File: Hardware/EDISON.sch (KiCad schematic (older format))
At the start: 5 parts, among them P5 CONN_01X06, SW2 PWR_BTN, U18 EdisonConnector

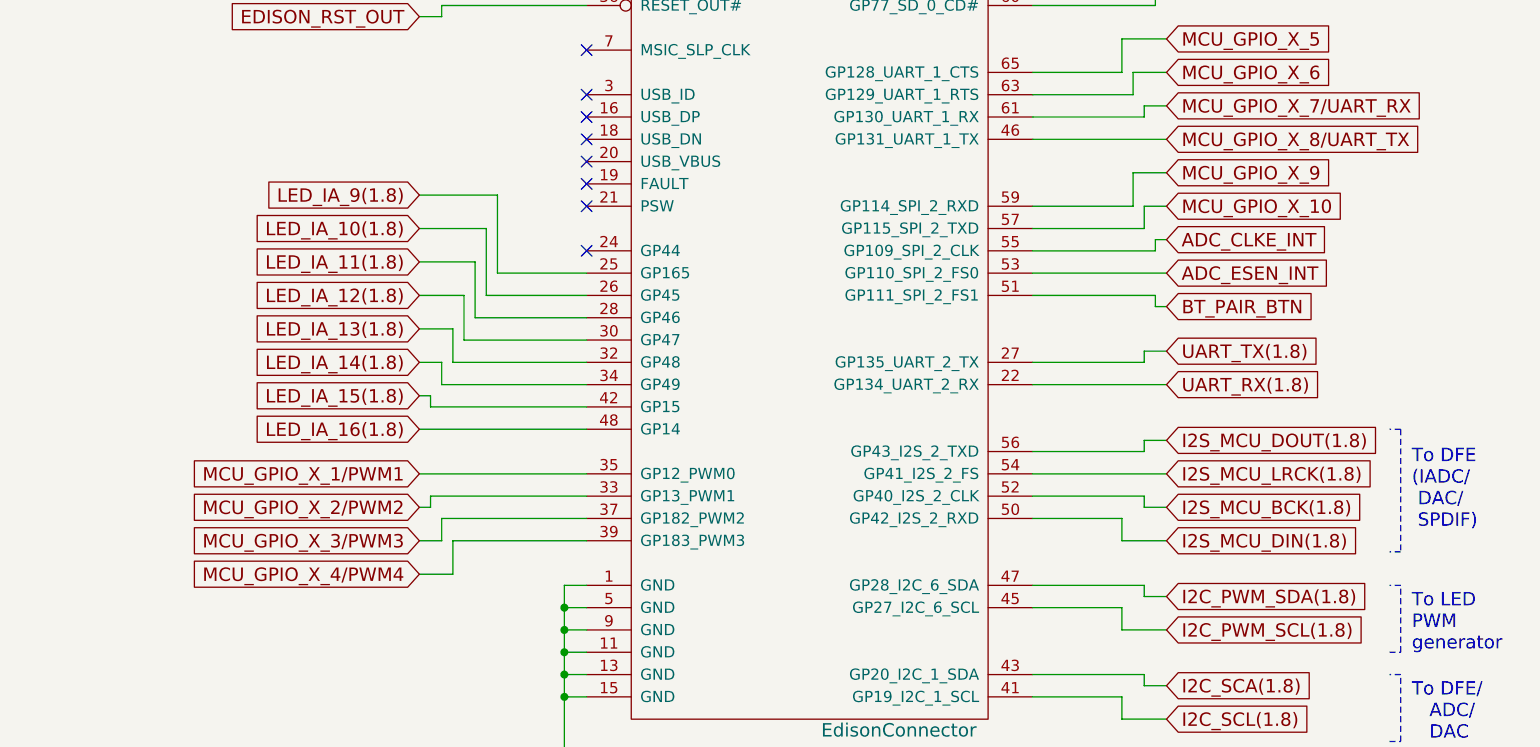
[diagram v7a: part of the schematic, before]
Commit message: Fixed schematic errors, added muse-v2-lib
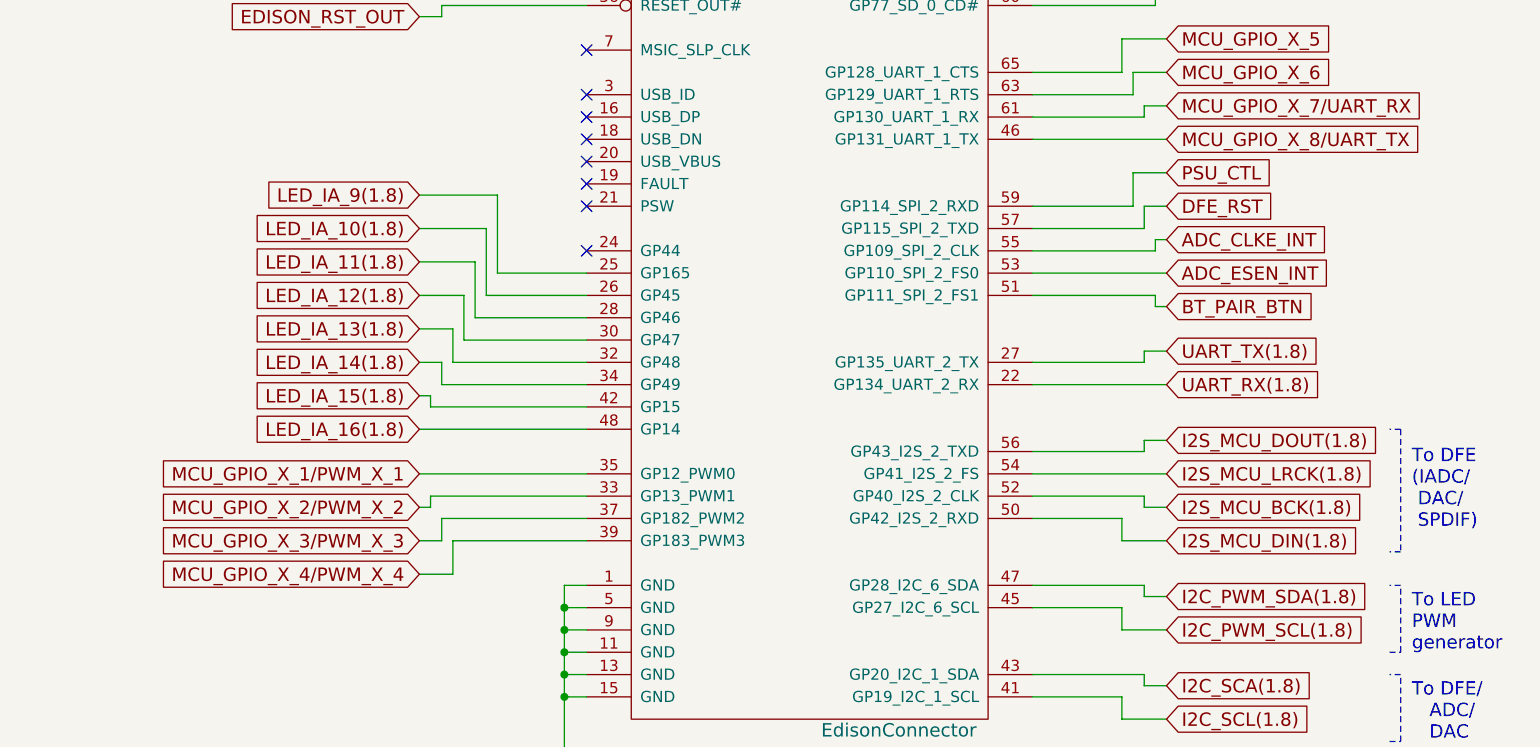
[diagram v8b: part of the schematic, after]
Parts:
- P5: footprint (none) -> Pin_Headers:Pin_Header_Straight_1x06
- R127, R128: footprint (none) -> Resistors_SMD:R_0402
- SW2: footprint (none) -> MF_Switches:MF_Switches-TACT4.2MM
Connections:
- net MCU_GPIO_X_1/PWM1 renamed MCU_GPIO_X_1/PWM_X_1
- net MCU_GPIO_X_10 renamed DFE_RST
- net MCU_GPIO_X_2/PWM2 renamed MCU_GPIO_X_2/PWM_X_2
- net MCU_GPIO_X_3/PWM3 renamed MCU_GPIO_X_3/PWM_X_3
- net MCU_GPIO_X_4/PWM4 renamed MCU_GPIO_X_4/PWM_X_4
- net MCU_GPIO_X_9 renamed PSU_CTL
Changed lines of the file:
@@
 F 0 "U18" H 3700 1600 60  0000 C CNN
 F 1 "EdisonConnector" H 4850 -3000 60  0000 C CNN
-F 2 "" H 3650 1950 60  0000 C CNN
+F 2 "" H 3650 1950 60  0001 C CNN
 F 3 "" H 3650 1950 60  0000 C CNN
 	1    3650 1550
@@
 To DFE\n(IADC/\n DAC/\n SPDIF)
 $Comp
-L +1.8VSB #PWR097
+L +1.8VSB #PWR106
 U 1 1 57F8CABA
 P 3150 1400
-F 0 "#PWR097" H 3150 1540 20  0001 C CNN
+F 0 "#PWR106" H 3150 1540 20  0001 C CNN
 F 1 "+1.8VSB" H 3150 1510 30  0000 C CNN
 F 2 "" H 3150 1400 60  0000 C CNN
@@
 $EndComp
 $Comp
-L +3.3VSB #PWR098
+L +3.3VSB #PWR107
 U 1 1 57F8CAC0
 P 3350 1400
-F 0 "#PWR098" H 3350 1360 30  0001 C CNN
+F 0 "#PWR107" H 3350 1360 30  0001 C CNN
 F 1 "+3.3VSB" H 3350 1510 30  0000 C CNN
 F 2 "" H 3350 1400 60  0000 C CNN
@@
 NoConn ~ 1250 1750
 $Comp
-L GND-RESCUE-museV2-RESCUE-museV2 #PWR099
+L GND-RESCUE-museV2-RESCUE-museV2 #PWR108
 U 1 1 57F8CACB
 P 1350 2050
-F 0 "#PWR099" H 1350 2050 30  0001 C CNN
+F 0 "#PWR108" H 1350 2050 30  0001 C CNN
 F 1 "GND" H 1350 1980 30  0001 C CNN
 F 2 "" H 1350 2050 60  0000 C CNN
@@
 F 0 "P5" H 1050 2050 50  0000 C CNN
 F 1 "CONN_01X06" V 1150 1700 50  0000 C CNN
-F 2 "" H 1050 1700 60  0000 C CNN
+F 2 "Pin_Headers:Pin_Header_Straight_1x06" H 1050 1700 60  0001 C CNN
 F 3 "" H 1050 1700 60  0000 C CNN
 	1    1050 1700
@@
 Intel Edison Connection
 $Comp
-L GND-RESCUE-museV2-RESCUE-museV2 #PWR0100
+L GND-RESCUE-museV2-RESCUE-museV2 #PWR109
 U 1 1 57F8CAEE
 P 3350 6200
-F 0 "#PWR0100" H 3350 6200 30  0001 C CNN
+F 0 "#PWR109" H 3350 6200 30  0001 C CNN
 F 1 "GND" H 3350 6130 30  0001 C CNN
 F 2 "" H 3350 6200 60  0000 C CNN
@@
 MCU_GPIO_X_8/UART_TX
 Text GLabel 6050 3600 2    60   Input ~ 0
-MCU_GPIO_X_9
+PSU_CTL
 Text GLabel 6050 3750 2    60   Input ~ 0
-MCU_GPIO_X_10
+DFE_RST
 Text GLabel 6050 3900 2    60   Input ~ 0
 ADC_CLKE_INT
@@
 	3050 3700 2700 3700
 Text GLabel 2700 4950 0    60   Input ~ 0
-MCU_GPIO_X_1/PWM1
+MCU_GPIO_X_1/PWM_X_1
 Wire Wire Line
 	2700 4950 3450 4950
 Text GLabel 2700 5100 0    60   Input ~ 0
-MCU_GPIO_X_2/PWM2
+MCU_GPIO_X_2/PWM_X_2
 Text GLabel 2700 5250 0    60   Input ~ 0
-MCU_GPIO_X_3/PWM3
+MCU_GPIO_X_3/PWM_X_3
 Text GLabel 2700 5400 0    60   Input ~ 0
-MCU_GPIO_X_4/PWM4
+MCU_GPIO_X_4/PWM_X_4
 Wire Wire Line
 	2700 5100 2750 5100
@@
 	2850 5250 3450 5250
 $Comp
-L GND-RESCUE-museV2-RESCUE-museV2 #PWR0101
+L GND-RESCUE-museV2-RESCUE-museV2 #PWR111
 U 1 1 58589956
 P 1150 8600
-F 0 "#PWR0101" H 1150 8600 30  0001 C CNN
+F 0 "#PWR111" H 1150 8600 30  0001 C CNN
 F 1 "GND" H 1150 8530 30  0001 C CNN
 F 2 "" H 1150 8600 60  0000 C CNN
@@
 F 0 "R127" V 1230 7200 40  0000 C CNN
 F 1 "10K" V 1157 7201 40  0000 C CNN
-F 2 "" V 1080 7200 30  0000 C CNN
+F 2 "Resistors_SMD:R_0402" V 1080 7200 30  0001 C CNN
 F 3 "" H 1150 7200 30  0000 C CNN
 	1    1150 7200
@@
 F 0 "SW2" H 1300 7960 50  0000 C CNN
 F 1 "PWR_BTN" H 1150 7770 50  0000 C CNN
-F 2 "" H 1150 7850 60  0000 C CNN
+F 2 "MF_Switches:MF_Switches-TACT4.2MM" H 1150 7850 60  0001 C CNN
 F 3 "" H 1150 7850 60  0000 C CNN
 	1    1150 7850
@@
 F 0 "R128" V 1430 7200 40  0000 C CNN
 F 1 "220" V 1357 7201 40  0000 C CNN
-F 2 "" V 1280 7200 30  0000 C CNN
+F 2 "Resistors_SMD:R_0402" V 1280 7200 30  0001 C CNN
 F 3 "" H 1350 7200 30  0000 C CNN
 	1    1350 7200
@@
 	1350 7450 1150 7450
 $Comp
-L +3.3VSB #PWR0102
+L +3.3VSB #PWR110
 U 1 1 58589976
 P 1150 6750
-F 0 "#PWR0102" H 1150 6710 30  0001 C CNN
+F 0 "#PWR110" H 1150 6710 30  0001 C CNN
 F 1 "+3.3VSB" H 1150 6860 30  0000 C CNN
 F 2 "" H 1150 6750 60  0000 C CNN
